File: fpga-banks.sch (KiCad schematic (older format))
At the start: 31 parts, among them J13 62000311121, U14 XC7A100T-FGG484

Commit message: Boot QSPI fixes, added status LEDs
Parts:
- added D? (x2): LG_L29K-G2J1-24-Z, artix-dc-scm-footprints:LED_0603, symbol artix-dc-scm:LG_L29K-G2J1-24-Z
- added Q? (x2): 2N7002, artix-dc-scm-footprints:SOT-23-3, symbol artix-dc-scm:2N7002
- added R?: R_2k2_0402, antmicro-footprints:0402-res, symbol antmicroResistors0402:R_2k2_0402
- added R? (x2): R_4k7_0402, antmicro-footprints:0402-res, symbol antmicroResistors0402:R_4k7_0402
- added R? (x2): R_1k_0402, artix-dc-scm-footprints:0402-res, symbol artix-dc-scm:R_1k_0402
- R2: renamed from R?; Populate (none) -> DNP
- R82, R83, R86, R87: Populate (none) -> DNP
- gave numbers to parts that had none: 1
- renumbered S1 to PROG_B
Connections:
- wire segments 288 -> 311
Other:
- note added: "Status LEDs"

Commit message: FPGA related fixes, removed floating tags from Interfaces
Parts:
- added D? (x3): LG_L29K-G2J1-24-Z, artix-dc-scm-footprints:LED_0603, symbol artix-dc-scm:LG_L29K-G2J1-24-Z
- added Q? (x3): 2N7002, artix-dc-scm-footprints:SOT-23-3, symbol artix-dc-scm:2N7002
- added R? (x3): R_1k_0402, artix-dc-scm-footprints:0402-res, symbol artix-dc-scm:R_1k_0402
- added TP? (x3): TP_SMD1MM, antmicro-footprints:Testpoint_smd_1mm, symbol antmicroTestPoints:TP_SMD1MM
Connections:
- net labels added: USR_LED0, USR_LED1, USR_LED2
- wire segments 311 -> 330
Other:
- moved on the sheet: D?, Q?, R?

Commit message: Fixes after review (pin connections)
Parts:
- R1, R2: symbol antmicroResistors0402:R_1k_0402 -> artix-dc-scm:R_1k_0402
- R133: renamed from R?; symbol antmicroResistors0402:R_2k2_0402 -> artix-dc-scm:R_2k2_0402
- R134, R135: renamed from R?; symbol antmicroResistors0402:R_4k7_0402 -> artix-dc-scm:R_4k7_0402
- TP2, TP5, TP6: renamed from TP?; symbol antmicroTestPoints:TP_SMD1MM -> artix-dc-scm:TP_SMD1MM
- gave numbers to parts that had none: 15
- renumbered PROG_B to PROG_B1
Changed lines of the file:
@@
 $EndComp
 $Comp
-L artix-dc-scm:KMR2 PROG_B
+L artix-dc-scm:KMR2 PROG_B1
 U 1 1 60DA2AC9
 P 10900 10100
-F 0 "PROG_B" V 10854 10238 50  0000 L CNN
+F 0 "PROG_B1" V 10854 10238 50  0000 L CNN
 F 1 "KMR2" V 10945 10238 50  0000 L CNN
 F 2 "artix-dc-scm-footprints:SW_SPST_4.2x2.8" H 11100 10300 50  0001 L CNN
@@
 PUDC_B
 $Comp
-L antmicroResistors0402:R_1k_0402 R1
+L artix-dc-scm:R_1k_0402 R1
 U 1 1 60F834C5
 P 7025 8350
@@
 $EndComp
 $Comp
-L antmicroResistors0402:R_1k_0402 R2
+L artix-dc-scm:R_1k_0402 R2
 U 1 1 60F84719
 P 7025 8800
@@
 	4550 2650 5025 2650
 $Comp
-L antmicroResistors0402:R_2k2_0402 R?
+L artix-dc-scm:R_2k2_0402 R133
 U 1 1 601DDEB8
 P 4625 1700
-F 0 "R?" V 4580 1770 60  0000 L CNN
+F 0 "R133" V 4580 1770 60  0000 L CNN
 F 1 "R_2k2_0402" H 4625 1550 60  0001 C CNN
 F 2 "antmicro-footprints:0402-res" H 4825 1900 60  0001 L CNN
@@
 $EndComp
 $Comp
-L antmicroResistors0402:R_4k7_0402 R?
+L artix-dc-scm:R_4k7_0402 R134
 U 1 1 601DFDEE
 P 4750 1700
-F 0 "R?" V 4705 1770 60  0000 L CNN
+F 0 "R134" V 4705 1770 60  0000 L CNN
 F 1 "R_4k7_0402" H 4750 1550 60  0001 C CNN
 F 2 "antmicro-footprints:0402-res" H 4950 1900 60  0001 L CNN
@@
 $EndComp
 $Comp
-L antmicroResistors0402:R_4k7_0402 R?
+L artix-dc-scm:R_4k7_0402 R135
 U 1 1 601E0616
 P 4875 1700
-F 0 "R?" V 4830 1770 60  0000 L CNN
+F 0 "R135" V 4830 1770 60  0000 L CNN
 F 1 "R_4k7_0402" H 4875 1550 60  0001 C CNN
 F 2 "antmicro-footprints:0402-res" H 5075 1900 60  0001 L CNN
@@
 P 4100 8500
 AR Path="/5FD86BEB/605CC5B1" Ref="D?"  Part="1"
-AR Path="/5FD86CE4/605CC5B1" Ref="D?"  Part="1"
-F 0 "D?" H 4125 8400 60  0000 L CNN
+AR Path="/5FD86CE4/605CC5B1" Ref="D9"  Part="1"
+F 0 "D9" H 4125 8400 60  0000 L CNN
 F 1 "LG_L29K-G2J1-24-Z" H 3225 8725 60  0000 L CNN
 F 2 "artix-dc-scm-footprints:LED_0603" H 4300 8700 60  0001 L CNN
@@
 P 4550 8500
 AR Path="/5FD86BEB/605CC5BC" Ref="R?"  Part="1"
-AR Path="/5FD86CE4/605CC5BC" Ref="R?"  Part="1"
-F 0 "R?" H 4500 8600 60  0000 C CNN
+AR Path="/5FD86CE4/605CC5BC" Ref="R128"  Part="1"
+F 0 "R128" H 4500 8600 60  0000 C CNN
 F 1 "R_1k_0402" H 4550 8350 60  0001 C CNN
 F 2 "artix-dc-scm-footprints:0402-res" H 4750 8700 60  0001 L CNN
@@
 P 3700 8500
 AR Path="/5FD86BEB/605CC5C6" Ref="Q?"  Part="1"
-AR Path="/5FD86CE4/605CC5C6" Ref="Q?"  Part="1"
-F 0 "Q?" V 3350 8500 60  0000 L CNN
+AR Path="/5FD86CE4/605CC5C6" Ref="Q12"  Part="1"
+F 0 "Q12" V 3350 8500 60  0000 L CNN
 F 1 "2N7002" V 3450 8500 60  0000 L CNN
 F 2 "artix-dc-scm-footprints:SOT-23-3" H 3900 8700 60  0001 L CNN
@@
 P 3375 8500
 AR Path="/5FD86BEB/605CC5CC" Ref="#PWR?"  Part="1"
-AR Path="/5FD86CE4/605CC5CC" Ref="#PWR?"  Part="1"
-F 0 "#PWR?" H 3375 8250 50  0001 C CNN
+AR Path="/5FD86CE4/605CC5CC" Ref="#PWR030"  Part="1"
+F 0 "#PWR030" H 3375 8250 50  0001 C CNN
 F 1 "GND" H 3380 8327 50  0000 C CNN
 F 2 "" H 3375 8500 50  0001 C CNN
@@
 P 4100 9050
 AR Path="/5FD86BEB/605FEFC2" Ref="D?"  Part="1"
-AR Path="/5FD86CE4/605FEFC2" Ref="D?"  Part="1"
-F 0 "D?" H 4125 8950 60  0000 L CNN
+AR Path="/5FD86CE4/605FEFC2" Ref="D10"  Part="1"
+F 0 "D10" H 4125 8950 60  0000 L CNN
 F 1 "LG_L29K-G2J1-24-Z" H 3225 9275 60  0000 L CNN
 F 2 "artix-dc-scm-footprints:LED_0603" H 4300 9250 60  0001 L CNN
@@
 P 4550 9050
 AR Path="/5FD86BEB/605FEFCD" Ref="R?"  Part="1"
-AR Path="/5FD86CE4/605FEFCD" Ref="R?"  Part="1"
-F 0 "R?" H 4500 9150 60  0000 C CNN
+AR Path="/5FD86CE4/605FEFCD" Ref="R129"  Part="1"
+F 0 "R129" H 4500 9150 60  0000 C CNN
 F 1 "R_1k_0402" H 4550 8900 60  0001 C CNN
 F 2 "artix-dc-scm-footprints:0402-res" H 4750 9250 60  0001 L CNN
@@
 P 3700 9050
 AR Path="/5FD86BEB/605FEFD7" Ref="Q?"  Part="1"
-AR Path="/5FD86CE4/605FEFD7" Ref="Q?"  Part="1"
-F 0 "Q?" V 3350 9050 60  0000 L CNN
+AR Path="/5FD86CE4/605FEFD7" Ref="Q13"  Part="1"
+F 0 "Q13" V 3350 9050 60  0000 L CNN
 F 1 "2N7002" V 3450 9050 60  0000 L CNN
 F 2 "artix-dc-scm-footprints:SOT-23-3" H 3900 9250 60  0001 L CNN
@@
 P 3400 9050
 AR Path="/5FD86BEB/605FEFDD" Ref="#PWR?"  Part="1"
-AR Path="/5FD86CE4/605FEFDD" Ref="#PWR?"  Part="1"
-F 0 "#PWR?" H 3400 8800 50  0001 C CNN
+AR Path="/5FD86CE4/605FEFDD" Ref="#PWR031"  Part="1"
+F 0 "#PWR031" H 3400 8800 50  0001 C CNN
 F 1 "GND" H 3405 8877 50  0000 C CNN
 F 2 "" H 3400 9050 50  0001 C CNN
@@
 Status LEDs
 $Comp
-L antmicroTestPoints:TP_SMD1MM TP?
+L artix-dc-scm:TP_SMD1MM TP2
 U 1 1 607DBFB7
 P 11050 9125
-F 0 "TP?" H 11075 9050 50  0000 R CNN
+F 0 "TP2" H 11075 9050 50  0000 R CNN
 F 1 "TP_SMD1MM" H 11050 9025 50  0001 C CNN
 F 2 "antmicro-footprints:Testpoint_smd_1mm" H 11250 9325 60  0001 L CNN
@@
 $EndComp
 $Comp
-L antmicroTestPoints:TP_SMD1MM TP?
+L artix-dc-scm:TP_SMD1MM TP5
 U 1 1 60868E72
 P 11175 9125
-F 0 "TP?" H 11175 9050 50  0000 R CNN
+F 0 "TP5" H 11175 9050 50  0000 R CNN
 F 1 "TP_SMD1MM" H 11175 9025 50  0001 C CNN
 F 2 "antmicro-footprints:Testpoint_smd_1mm" H 11375 9325 60  0001 L CNN
@@
 $EndComp
 $Comp
-L antmicroTestPoints:TP_SMD1MM TP?
+L artix-dc-scm:TP_SMD1MM TP6
 U 1 1 60869265
 P 11300 9125
-F 0 "TP?" H 11275 9050 50  0000 R CNN
+F 0 "TP6" H 11275 9050 50  0000 R CNN
 F 1 "TP_SMD1MM" H 11300 9025 50  0001 C CNN
 F 2 "antmicro-footprints:Testpoint_smd_1mm" H 11500 9325 60  0001 L CNN
@@
 P 4100 9625
 AR Path="/5FD86BEB/60D22676" Ref="D?"  Part="1"
-AR Path="/5FD86CE4/60D22676" Ref="D?"  Part="1"
-F 0 "D?" H 4125 9525 60  0000 L CNN
+AR Path="/5FD86CE4/60D22676" Ref="D11"  Part="1"
+F 0 "D11" H 4125 9525 60  0000 L CNN
 F 1 "LG_L29K-G2J1-24-Z" H 3225 9850 60  0000 L CNN
 F 2 "artix-dc-scm-footprints:LED_0603" H 4300 9825 60  0001 L CNN
@@
 P 4550 9625
 AR Path="/5FD86BEB/60D22681" Ref="R?"  Part="1"
-AR Path="/5FD86CE4/60D22681" Ref="R?"  Part="1"
-F 0 "R?" H 4500 9725 60  0000 C CNN
+AR Path="/5FD86CE4/60D22681" Ref="R130"  Part="1"
+F 0 "R130" H 4500 9725 60  0000 C CNN
 F 1 "R_1k_0402" H 4550 9475 60  0001 C CNN
 F 2 "artix-dc-scm-footprints:0402-res" H 4750 9825 60  0001 L CNN
@@
 P 3700 9625
 AR Path="/5FD86BEB/60D2268B" Ref="Q?"  Part="1"
-AR Path="/5FD86CE4/60D2268B" Ref="Q?"  Part="1"
-F 0 "Q?" V 3350 9625 60  0000 L CNN
+AR Path="/5FD86CE4/60D2268B" Ref="Q14"  Part="1"
+F 0 "Q14" V 3350 9625 60  0000 L CNN
 F 1 "2N7002" V 3450 9625 60  0000 L CNN
 F 2 "artix-dc-scm-footprints:SOT-23-3" H 3900 9825 60  0001 L CNN
@@
 P 3400 9625
 AR Path="/5FD86BEB/60D22691" Ref="#PWR?"  Part="1"
-AR Path="/5FD86CE4/60D22691" Ref="#PWR?"  Part="1"
-F 0 "#PWR?" H 3400 9375 50  0001 C CNN
+AR Path="/5FD86CE4/60D22691" Ref="#PWR033"  Part="1"
+F 0 "#PWR033" H 3400 9375 50  0001 C CNN
 F 1 "GND" H 3405 9452 50  0000 C CNN
 F 2 "" H 3400 9625 50  0001 C CNN
@@
 P 4100 10225
 AR Path="/5FD86BEB/60D56405" Ref="D?"  Part="1"
-AR Path="/5FD86CE4/60D56405" Ref="D?"  Part="1"
-F 0 "D?" H 4125 10125 60  0000 L CNN
+AR Path="/5FD86CE4/60D56405" Ref="D12"  Part="1"
+F 0 "D12" H 4125 10125 60  0000 L CNN
 F 1 "LG_L29K-G2J1-24-Z" H 3225 10450 60  0000 L CNN
 F 2 "artix-dc-scm-footprints:LED_0603" H 4300 10425 60  0001 L CNN
@@
 P 4550 10225
 AR Path="/5FD86BEB/60D56410" Ref="R?"  Part="1"
-AR Path="/5FD86CE4/60D56410" Ref="R?"  Part="1"
-F 0 "R?" H 4500 10325 60  0000 C CNN
+AR Path="/5FD86CE4/60D56410" Ref="R131"  Part="1"
+F 0 "R131" H 4500 10325 60  0000 C CNN
 F 1 "R_1k_0402" H 4550 10075 60  0001 C CNN
 F 2 "artix-dc-scm-footprints:0402-res" H 4750 10425 60  0001 L CNN
@@
 P 3700 10225
 AR Path="/5FD86BEB/60D5641A" Ref="Q?"  Part="1"
-AR Path="/5FD86CE4/60D5641A" Ref="Q?"  Part="1"
-F 0 "Q?" V 3350 10225 60  0000 L CNN
+AR Path="/5FD86CE4/60D5641A" Ref="Q15"  Part="1"
+F 0 "Q15" V 3350 10225 60  0000 L CNN
 F 1 "2N7002" V 3450 10225 60  0000 L CNN
 F 2 "artix-dc-scm-footprints:SOT-23-3" H 3900 10425 60  0001 L CNN
@@
 P 3400 10225
 AR Path="/5FD86BEB/60D56420" Ref="#PWR?"  Part="1"
-AR Path="/5FD86CE4/60D56420" Ref="#PWR?"  Part="1"
-F 0 "#PWR?" H 3400 9975 50  0001 C CNN
+AR Path="/5FD86CE4/60D56420" Ref="#PWR035"  Part="1"
+F 0 "#PWR035" H 3400 9975 50  0001 C CNN
 F 1 "GND" H 3405 10052 50  0000 C CNN
 F 2 "" H 3400 10225 50  0001 C CNN
@@
 P 4100 10825
 AR Path="/5FD86BEB/60EC059F" Ref="D?"  Part="1"
-AR Path="/5FD86CE4/60EC059F" Ref="D?"  Part="1"
-F 0 "D?" H 4125 10725 60  0000 L CNN
+AR Path="/5FD86CE4/60EC059F" Ref="D13"  Part="1"
+F 0 "D13" H 4125 10725 60  0000 L CNN
 F 1 "LG_L29K-G2J1-24-Z" H 3225 11050 60  0000 L CNN
 F 2 "artix-dc-scm-footprints:LED_0603" H 4300 11025 60  0001 L CNN
@@
 P 4550 10825
 AR Path="/5FD86BEB/60EC05AA" Ref="R?"  Part="1"
-AR Path="/5FD86CE4/60EC05AA" Ref="R?"  Part="1"
-F 0 "R?" H 4500 10925 60  0000 C CNN
+AR Path="/5FD86CE4/60EC05AA" Ref="R132"  Part="1"
+F 0 "R132" H 4500 10925 60  0000 C CNN
 F 1 "R_1k_0402" H 4550 10675 60  0001 C CNN
 F 2 "artix-dc-scm-footprints:0402-res" H 4750 11025 60  0001 L CNN
@@
 P 3700 10825
 AR Path="/5FD86BEB/60EC05B4" Ref="Q?"  Part="1"
-AR Path="/5FD86CE4/60EC05B4" Ref="Q?"  Part="1"
-F 0 "Q?" V 3350 10825 60  0000 L CNN
+AR Path="/5FD86CE4/60EC05B4" Ref="Q16"  Part="1"
+F 0 "Q16" V 3350 10825 60  0000 L CNN
 F 1 "2N7002" V 3450 10825 60  0000 L CNN
 F 2 "artix-dc-scm-footprints:SOT-23-3" H 3900 11025 60  0001 L CNN
@@
 P 3400 10825
 AR Path="/5FD86BEB/60EC05BA" Ref="#PWR?"  Part="1"
-AR Path="/5FD86CE4/60EC05BA" Ref="#PWR?"  Part="1"
-F 0 "#PWR?" H 3400 10575 50  0001 C CNN
+AR Path="/5FD86CE4/60EC05BA" Ref="#PWR091"  Part="1"
+F 0 "#PWR091" H 3400 10575 50  0001 C CNN
 F 1 "GND" H 3405 10652 50  0000 C CNN
 F 2 "" H 3400 10825 50  0001 C CNN

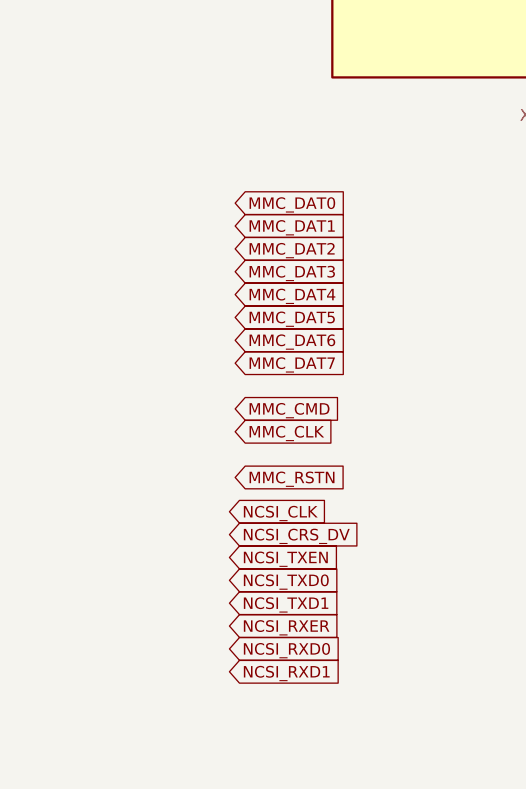
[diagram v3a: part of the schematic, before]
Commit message: Added USB client chip
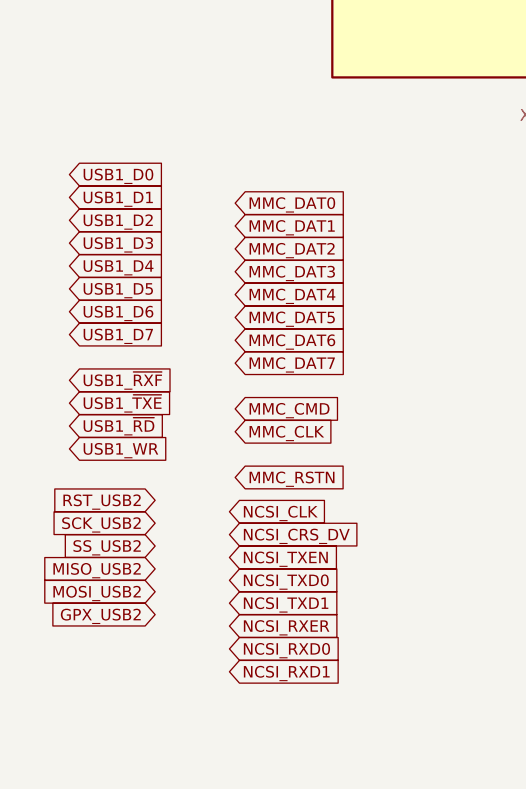
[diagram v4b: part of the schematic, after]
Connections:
- net labels added: GPX_USB2, MISO_USB2, MOSI_USB2, RST_USB2, SCK_USB2, SS_USB2, USB1_D0, USB1_D1, USB1_D2, USB1_D3, USB1_D4, USB1_D5, USB1_D6, USB1_D7, USB1_WR, USB1_~RD, USB1_~RXF, USB1_~TXE
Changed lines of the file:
@@
 Text GLabel 15925 6250 0    50   Input ~ 0
 USR_LED2
+Text GLabel 850  7475 2    50   Input ~ 0
+USB1_D0
+Text GLabel 850  7575 2    50   Input ~ 0
+USB1_D1
+Text GLabel 850  7675 2    50   Input ~ 0
+USB1_D2
+Text GLabel 850  7775 2    50   Input ~ 0
+USB1_D3
+Text GLabel 850  7875 2    50   Input ~ 0
+USB1_D4
+Text GLabel 850  7975 2    50   Input ~ 0
+USB1_D5
+Text GLabel 850  8075 2    50   Input ~ 0
+USB1_D6
+Text GLabel 850  8175 2    50   Input ~ 0
+USB1_D7
+Text GLabel 850  8375 2    50   Input ~ 0
+USB1_~RXF
+Text GLabel 850  8475 2    50   Input ~ 0
+USB1_~TXE
+Text GLabel 850  8575 2    50   Input ~ 0
+USB1_~RD
+Text GLabel 850  8675 2    50   Input ~ 0
+USB1_WR
+Text GLabel 1225 8900 0    50   Input ~ 0
+RST_USB2
+Text GLabel 1225 9000 0    50   Input ~ 0
+SCK_USB2
+Text GLabel 1225 9100 0    50   Input ~ 0
+SS_USB2
+Text GLabel 1225 9200 0    50   Input ~ 0
+MISO_USB2
+Text GLabel 1225 9300 0    50   Input ~ 0
+MOSI_USB2
+Text GLabel 1225 9400 0    50   Input ~ 0
+GPX_USB2
 $EndSCHEMATC
